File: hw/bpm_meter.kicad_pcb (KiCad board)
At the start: 2 copper layers, 55 x 73.5 mm, 92 parts, among them J1 weidmueller_SL5.08HC-06-90, J2 weidmueller_SL5.08HC-10-90, J901 USB_C_Receptacle_USB2.0, Q1 AO3400A, SW1 dip_switch_SPST16, SW901 SW_MEC_5E, U1 SP3485EN-L/TR, U2 AOZ1282CI, U901 RP2040, U902 AMS1117-3.3, U903 W25Q128JVS, Y901 Crystal_GND24_Small

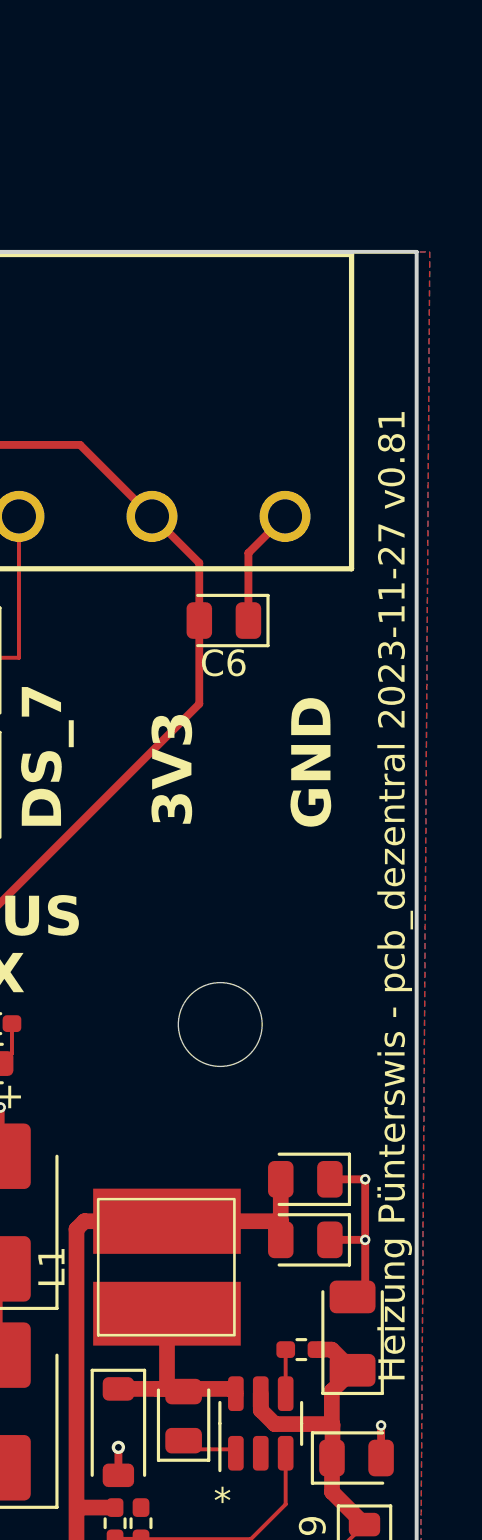
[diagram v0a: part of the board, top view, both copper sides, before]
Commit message: Renamed the KiCad project
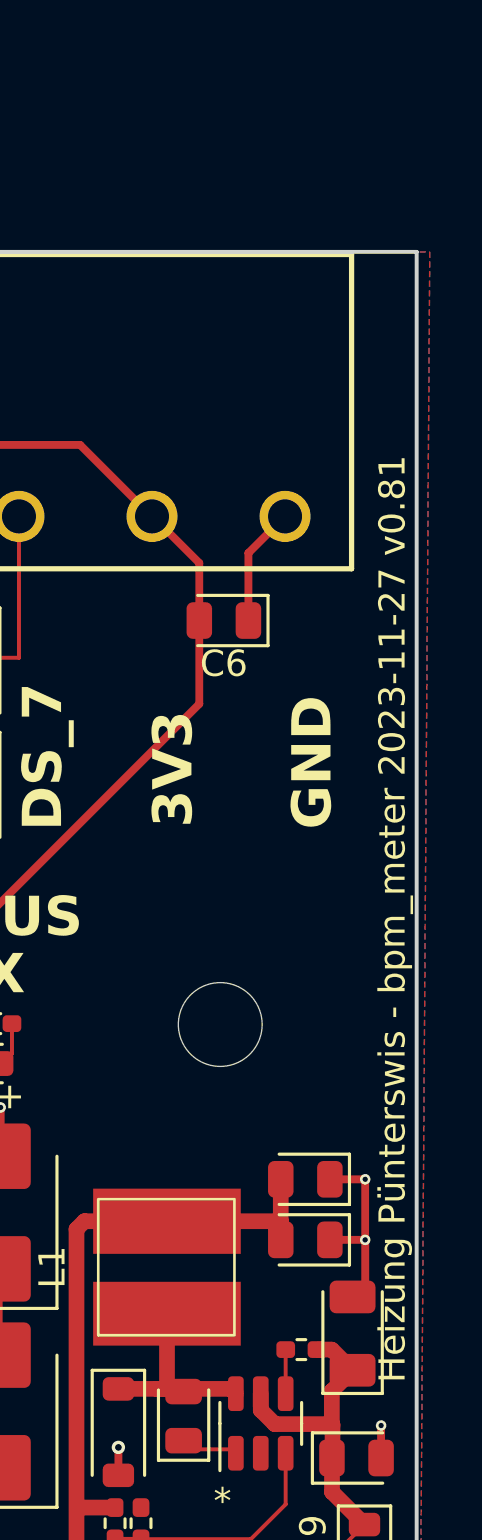
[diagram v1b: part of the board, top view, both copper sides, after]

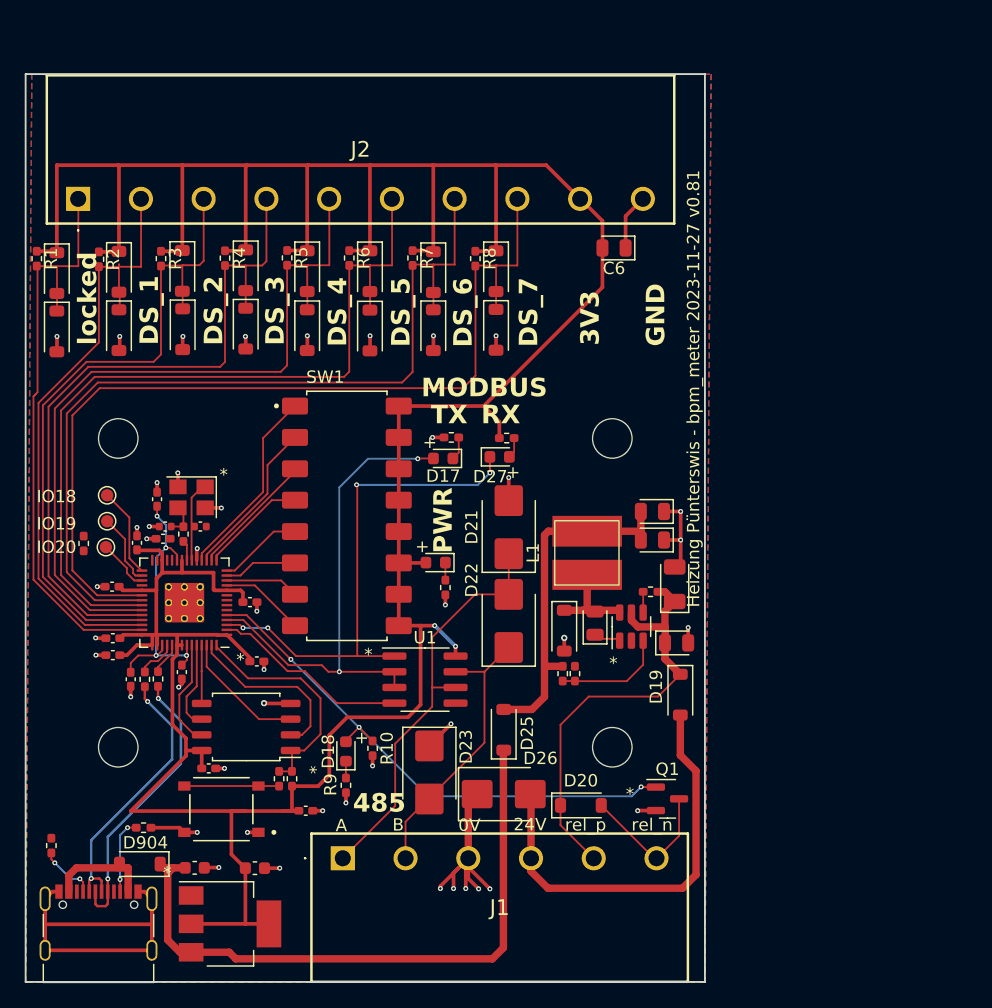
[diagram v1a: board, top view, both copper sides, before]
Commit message: Removed unused stuff and added beat input
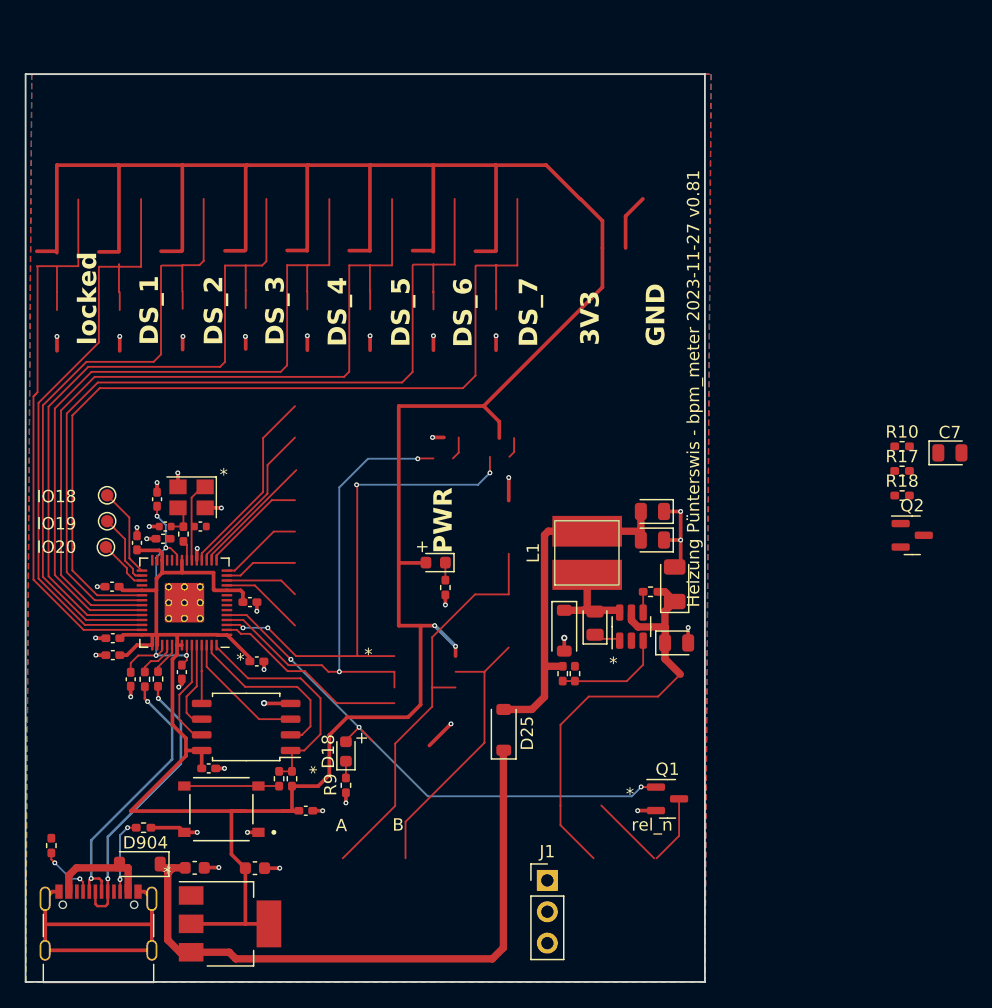
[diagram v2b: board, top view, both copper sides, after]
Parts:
- removed C6: 100n 50V, Diode_SMD:D_0805_2012Metric
- removed D1, D10, D11, D12, D13, D14, D15, D16, D19, D2, D20, D3, D4, D5, D6, D7, D8, D9: B5819W SL, Diode_SMD:D_SOD-123
- removed D17: LED RED, 00_project_library:LED_0603_1608Metric
- removed D21, D22, D23: SMBJ6.5CA, Diode_SMD:D_SMB
- removed D26: SMBJ30CA, Diode_SMD:D_SMB
- removed D27: LED BLUE, 00_project_library:LED_0603_1608Metric
- removed HOLDER1: ~, 00_project_library:din_rail_pcb_holder
- removed J2: weidmueller_SL5.08HC-10-90, 00_project_library:weidmueller_SL5.08HC-10-90
- removed R1, R14, R2, R3, R4, R5, R6, R7, R8: 4k7, Resistor_SMD:R_0402_1005Metric_Pad0.72x0.64mm_HandSolder
- removed R15, R16: 470R, Resistor_SMD:R_0402_1005Metric_Pad0.72x0.64mm_HandSolder
- removed SW1: dip_switch_SPST16, 00_project_library:dip_switch_SPST16
- removed U1: SP3485EN-L/TR, Package_SO:SOIC-8_3.9x4.9mm_P1.27mm
- added C7: 100n 50V, Diode_SMD:D_0805_2012Metric, F.Cu at (148.8, 89.7)
- added Q2: AO3400A, Package_TO_SOT_SMD:SOT-23, F.Cu at (145.8, 96.3)
- added R17: 10k, Resistor_SMD:R_0402_1005Metric_Pad0.72x0.64mm_HandSolder, F.Cu at (145.0, 91.1)
- added R18: 10k, Resistor_SMD:R_0402_1005Metric_Pad0.72x0.64mm_HandSolder, F.Cu at (145.0, 93.1)
- J1: value weidmueller_SL5.08HC-06-90 -> Conn_01x03_Pin; footprint 00_project_library:weidmueller_SL5.08HC-06-90 -> Connector_PinHeader_2.54mm:PinHeader_1x03_P2.54mm_Vertical
- R10: value 10k -> 4k7
- moved R10 49.4 mm to (145.0, 89.1), turned to 0 degrees
- moved J1 16.7 mm to (116.2, 124.3)
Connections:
- C1 pad 1: 24Vp -> +14V
- C2 pad 1: 24Vp -> +14V
- D18 pad 2: rel -> +5V
- J1 pad 1: 485_A -> +14V
- J1 pad 2: 485_B -> Net-(J1-Pin_2)
- Q1 pad 1: rel -> Net-(Q1-G)
- Q1 pad 3: rel_n -> beat_3V3
- R10 pad 1: rel -> Net-(Q1-G)
- R11 pad 1: 24Vp -> +14V
- R9 pad 2: GND -> Net-(Q2-D)
- U2 pad 5: 24Vp -> +14V
- U901 pad 11: modbus_addr_7 -> unconnected-(U901-GPIO8-Pad11)
- U901 pad 12: modbus_addr_6 -> unconnected-(U901-GPIO9-Pad12)
- U901 pad 13: modbus_addr_5 -> unconnected-(U901-GPIO10-Pad13)
- U901 pad 14: modbus_addr_4 -> unconnected-(U901-GPIO11-Pad14)
- U901 pad 15: modbus_addr_3 -> unconnected-(U901-GPIO12-Pad15)
- U901 pad 16: modbus_addr_2 -> unconnected-(U901-GPIO13-Pad16)
- U901 pad 17: modbus_addr_1 -> unconnected-(U901-GPIO14-Pad17)
- U901 pad 18: modbus_addr_0 -> unconnected-(U901-GPIO15-Pad18)
- U901 pad 2: MODBUS_DI -> beat_3V3
- U901 pad 3: MODBUS_RO -> unconnected-(U901-GPIO1-Pad3)
- U901 pad 34: ds_7 -> unconnected-(U901-GPIO22-Pad34)
- U901 pad 35: ds_6 -> unconnected-(U901-GPIO23-Pad35)
- U901 pad 36: ds_5 -> unconnected-(U901-GPIO24-Pad36)
- U901 pad 37: ds_4 -> unconnected-(U901-GPIO25-Pad37)
- U901 pad 38: ds_3 -> unconnected-(U901-GPIO26/ADC0-Pad38)
- U901 pad 39: ds_2 -> unconnected-(U901-GPIO27/ADC1-Pad39)
- U901 pad 4: MODBUS_DE -> unconnected-(U901-GPIO2-Pad4)
- U901 pad 40: ds_1 -> unconnected-(U901-GPIO28/ADC2-Pad40)
- U901 pad 41: ds_0 -> unconnected-(U901-GPIO29/ADC3-Pad41)
- U901 pad 5: rel -> unconnected-(U901-GPIO3-Pad5)
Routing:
- net (no net): track 0.00 -> 110.4 mm
- net unconnected-(U901-GPIO22-Pad34): track 0.00 -> 74.3 mm
- net ds_7: track 74.3 -> 0.00 mm
- net unconnected-(U901-GPIO23-Pad35): track 0.00 -> 70.3 mm
- net ds_6: track 70.3 -> 0.00 mm
- net unconnected-(U901-GPIO24-Pad36): track 0.00 -> 66.5 mm
- net ds_5: track 66.5 -> 0.00 mm
- net unconnected-(U901-GPIO25-Pad37): track 0.00 -> 62.5 mm
- net ds_4: track 62.5 -> 0.00 mm
- net unconnected-(U901-GPIO26/ADC0-Pad38): track 0.00 -> 58.2 mm
- net ds_3: track 58.2 -> 0.00 mm
- net unconnected-(U901-GPIO27/ADC1-Pad39): track 0.00 -> 53.8 mm
- net ds_2: track 53.8 -> 0.00 mm
- net unconnected-(U901-GPIO28/ADC2-Pad40): track 0.00 -> 50.1 mm
- net ds_1: track 50.1 -> 0.00 mm
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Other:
- board text removed: "0V"
- board text removed: "24V"
- board text removed: "485"
- board text removed: "MODBUS"
- board text removed: "RX"
- board text removed: "TX"
- board text removed: "rel_p"

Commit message: Export to PCB
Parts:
- removed D18: LED WHITE, 00_project_library:LED_0603_1608Metric
- removed IO18, IO19, IO20: TestPoint, TestPoint:TestPoint_Pad_D1.0mm
- added C10: 100n, Capacitor_SMD:C_0402_1005Metric, F.Cu at (215.6, 109.6)
- added C11: 1u, Capacitor_SMD:C_0402_1005Metric, F.Cu at (218.4, 101.7)
- added C12: 1u, Capacitor_SMD:C_0402_1005Metric, F.Cu at (218.4, 103.7)
- added C13: 100n, Capacitor_SMD:C_0402_1005Metric, F.Cu at (218.4, 105.7)
- added C14: 100n, Capacitor_SMD:C_0402_1005Metric, F.Cu at (218.4, 107.6)
- added C15: 1u, Capacitor_SMD:C_0402_1005Metric, F.Cu at (218.4, 109.6)
- added C16: 1u, Capacitor_SMD:C_0402_1005Metric, F.Cu at (221.3, 101.7)
- added C17: 100n, Capacitor_SMD:C_0402_1005Metric, F.Cu at (221.3, 103.7)
- added C18: 100n, Capacitor_SMD:C_0402_1005Metric, F.Cu at (221.3, 105.7)
- added C6: 1u, Capacitor_SMD:C_0402_1005Metric, F.Cu at (215.6, 101.7)
- added C8: 1u, Capacitor_SMD:C_0402_1005Metric, F.Cu at (215.6, 105.7)
- added C9: 100n, Capacitor_SMD:C_0402_1005Metric, F.Cu at (215.6, 107.6)
- added Q10: DMN2004VK, Package_TO_SOT_SMD:SOT-563, F.Cu at (223.5, 118.7)
- added Q11: DMN2004VK, Package_TO_SOT_SMD:SOT-563, F.Cu at (227.2, 112.2)
- added Q12: DMN2004VK, Package_TO_SOT_SMD:SOT-563, F.Cu at (227.2, 115.5)
- added Q13: DMN2004VK, Package_TO_SOT_SMD:SOT-563, F.Cu at (227.2, 118.7)
- added Q3: DMN2004VK, Package_TO_SOT_SMD:SOT-563, F.Cu at (216.0, 115.5)
- added Q4: DMN2004VK, Package_TO_SOT_SMD:SOT-563, F.Cu at (216.0, 118.7)
- added Q5: DMN2004VK, Package_TO_SOT_SMD:SOT-563, F.Cu at (219.8, 112.2)
- added Q6: DMN2004VK, Package_TO_SOT_SMD:SOT-563, F.Cu at (219.8, 115.5)
- added Q7: DMN2004VK, Package_TO_SOT_SMD:SOT-563, F.Cu at (219.8, 118.7)
- added Q8: DMN2004VK, Package_TO_SOT_SMD:SOT-563, F.Cu at (223.5, 112.2)
- added Q9: DMN2004VK, Package_TO_SOT_SMD:SOT-563, F.Cu at (223.5, 115.5)
- added R1: 4k7, Resistor_SMD:R_0402_1005Metric_Pad0.72x0.64mm_HandSolder, F.Cu at (215.8, 87.8)
- added R14: 220, Resistor_SMD:R_0402_1005Metric_Pad0.72x0.64mm_HandSolder, F.Cu at (219.0, 91.8)
- added R15: 220, Resistor_SMD:R_0402_1005Metric_Pad0.72x0.64mm_HandSolder, F.Cu at (219.0, 93.8)
- added R16: 220, Resistor_SMD:R_0402_1005Metric_Pad0.72x0.64mm_HandSolder, F.Cu at (219.0, 95.8)
- added R19: 220, Resistor_SMD:R_0402_1005Metric_Pad0.72x0.64mm_HandSolder, F.Cu at (219.0, 97.7)
- added R2: 220, Resistor_SMD:R_0402_1005Metric_Pad0.72x0.64mm_HandSolder, F.Cu at (215.8, 89.8)
- added R20: 220, Resistor_SMD:R_0402_1005Metric_Pad0.72x0.64mm_HandSolder, F.Cu at (219.0, 99.7)
- added R21: 220, Resistor_SMD:R_0402_1005Metric_Pad0.72x0.64mm_HandSolder, F.Cu at (222.2, 87.8)
- added R22: 220, Resistor_SMD:R_0402_1005Metric_Pad0.72x0.64mm_HandSolder, F.Cu at (222.2, 89.8)
- added R23: 220, Resistor_SMD:R_0402_1005Metric_Pad0.72x0.64mm_HandSolder, F.Cu at (222.2, 91.8)
- added R24: 220, Resistor_SMD:R_0402_1005Metric_Pad0.72x0.64mm_HandSolder, F.Cu at (222.2, 93.8)
- added R25: 220, Resistor_SMD:R_0402_1005Metric_Pad0.72x0.64mm_HandSolder, F.Cu at (222.2, 95.8)
- added R26: 220, Resistor_SMD:R_0402_1005Metric_Pad0.72x0.64mm_HandSolder, F.Cu at (222.2, 97.7)
- added R27: 220, Resistor_SMD:R_0402_1005Metric_Pad0.72x0.64mm_HandSolder, F.Cu at (222.2, 99.7)
- added R28: 220, Resistor_SMD:R_0402_1005Metric_Pad0.72x0.64mm_HandSolder, F.Cu at (225.5, 87.8)
- added R29: 220, Resistor_SMD:R_0402_1005Metric_Pad0.72x0.64mm_HandSolder, F.Cu at (225.5, 89.8)
- added R3: 220, Resistor_SMD:R_0402_1005Metric_Pad0.72x0.64mm_HandSolder, F.Cu at (215.8, 91.8)
- added R30: 220, Resistor_SMD:R_0402_1005Metric_Pad0.72x0.64mm_HandSolder, F.Cu at (225.5, 91.8)
- added R31: 220, Resistor_SMD:R_0402_1005Metric_Pad0.72x0.64mm_HandSolder, F.Cu at (225.5, 93.8)
- added R4: 220, Resistor_SMD:R_0402_1005Metric_Pad0.72x0.64mm_HandSolder, F.Cu at (215.8, 93.8)
- added R5: 220, Resistor_SMD:R_0402_1005Metric_Pad0.72x0.64mm_HandSolder, F.Cu at (215.8, 95.8)
- added R6: 220, Resistor_SMD:R_0402_1005Metric_Pad0.72x0.64mm_HandSolder, F.Cu at (215.8, 97.7)
- added R7: 220, Resistor_SMD:R_0402_1005Metric_Pad0.72x0.64mm_HandSolder, F.Cu at (215.8, 99.7)
- added R8: 220, Resistor_SMD:R_0402_1005Metric_Pad0.72x0.64mm_HandSolder, F.Cu at (219.0, 87.8)
- added U1: SLS0391FR1A1GD, 00_project_library:SLS0391, F.Cu at (223.2, 59.2)
- added U3: H11L1, 00_project_library:SOP-6-2.54mm, F.Cu at (164.2, 120.7)
- added U4: SLS0391FR1A1GD, 00_project_library:SLS0391, F.Cu at (223.2, 70.2)
- added U5: SLS0391FR1A1GD, 00_project_library:SLS0391, F.Cu at (223.2, 81.3)
- C7: value 100n 50V -> 100n; footprint Diode_SMD:D_0805_2012Metric -> Capacitor_SMD:C_0402_1005Metric
- J1: footprint Connector_PinHeader_2.54mm:PinHeader_1x03_P2.54mm_Vertical -> Connector_PinHeader_2.54mm:PinHeader_1x05_P2.54mm_Vertical
- Q2: value AO3400A -> DMN2004VK; footprint Package_TO_SOT_SMD:SOT-23 -> Package_TO_SOT_SMD:SOT-563
- R9: value 470 -> 220
- moved R9 122.0 mm to (219.0, 89.8), turned to 0 degrees
- moved Q2 72.0 mm to (216.0, 112.2)
- moved C7 68.2 mm to (215.6, 103.7)
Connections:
- C7 pad 1: Net-(Q1-G) -> +5V
- J1 pad 3: GND -> Net-(J1-Pin_3)
- Q1 pad 3: beat_3V3 -> beat_od
- Q2 pad 1: beat_3V3 -> GND
- Q2 pad 2: GND -> led_1A
- Q2 pad 3: Net-(Q2-D) -> Net-(Q2-D2)
- R17 pad 1: Net-(J1-Pin_2) -> Net-(Q1-G)
- R17 pad 2: Net-(Q1-G) -> Net-(J1-Pin_2)
- R18 pad 2: beat_3V3 -> beat_od
- R9 pad 2: Net-(Q2-D) -> Net-(Q5-D2)
- U901 pad 11: unconnected-(U901-GPIO8-Pad11) -> led_2A
- U901 pad 12: unconnected-(U901-GPIO9-Pad12) -> led_2B
- U901 pad 13: unconnected-(U901-GPIO10-Pad13) -> led_2C
- U901 pad 14: unconnected-(U901-GPIO11-Pad14) -> led_2D
- U901 pad 15: unconnected-(U901-GPIO12-Pad15) -> led_2E
- U901 pad 16: unconnected-(U901-GPIO13-Pad16) -> led_2F
- U901 pad 17: unconnected-(U901-GPIO14-Pad17) -> led_2G
- U901 pad 18: unconnected-(U901-GPIO15-Pad18) -> led_2P
- U901 pad 2: beat_3V3 -> led_1A
- U901 pad 27: unconnected-(U901-GPIO16-Pad27) -> led_3A
- U901 pad 28: unconnected-(U901-GPIO17-Pad28) -> led_3B
- U901 pad 29: Net-(U901-GPIO18) -> led_3C
- U901 pad 3: unconnected-(U901-GPIO1-Pad3) -> led_1B
- U901 pad 30: Net-(U901-GPIO19) -> led_3D
- U901 pad 31: Net-(U901-GPIO20) -> led_3E
- U901 pad 32: unconnected-(U901-GPIO21-Pad32) -> led_3F
- U901 pad 34: unconnected-(U901-GPIO22-Pad34) -> led_3G
- U901 pad 35: unconnected-(U901-GPIO23-Pad35) -> led_3P
- U901 pad 36: unconnected-(U901-GPIO24-Pad36) -> beat_od
- U901 pad 37: unconnected-(U901-GPIO25-Pad37) -> beat_opto
- U901 pad 4: unconnected-(U901-GPIO2-Pad4) -> led_1C
- U901 pad 5: unconnected-(U901-GPIO3-Pad5) -> led_1D
- U901 pad 6: unconnected-(U901-GPIO4-Pad6) -> led_1E
- U901 pad 7: unconnected-(U901-GPIO5-Pad7) -> led_1F
- U901 pad 8: unconnected-(U901-GPIO6-Pad8) -> led_1G
- U901 pad 9: unconnected-(U901-GPIO7-Pad9) -> led_1P
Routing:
- net +3V3: track 282.5 -> 138.8 mm
- net unconnected-(U901-GPIO22-Pad34): track 74.3 -> 0.00 mm
- net unconnected-(U901-GPIO23-Pad35): track 70.3 -> 0.00 mm
- net unconnected-(U901-GPIO24-Pad36): track 66.5 -> 0.00 mm
- net unconnected-(U901-GPIO25-Pad37): track 62.5 -> 0.00 mm
- net unconnected-(U901-GPIO1-Pad3): track 41.0 -> 0.00 mm, vias 4 -> 0
- net unconnected-(U901-GPIO2-Pad4): track 40.1 -> 0.00 mm, vias 2 -> 0
- net unconnected-(U901-GPIO26/ADC0-Pad38): track 58.2 -> 22.6 mm
- net unconnected-(U901-GPIO27/ADC1-Pad39): track 53.8 -> 23.3 mm
- net beat_od: track 0.00 -> 26.5 mm
- net unconnected-(U901-GPIO28/ADC2-Pad40): track 50.1 -> 24.2 mm
- net unconnected-(U901-GPIO29/ADC3-Pad41): track 48.2 -> 25.3 mm
- net beat_opto: track 0.00 -> 21.7 mm
- net beat_3V3: track 21.6 -> 0.00 mm
- net led_3P: track 0.00 -> 19.9 mm
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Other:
- board text removed: "3V3"
- board text removed: "DS_1"
- board text removed: "DS_2"
- board text removed: "DS_3"
- board text removed: "DS_4"
- board text removed: "DS_5"
- board text removed: "DS_6"
- board text removed: "DS_7"
- board text removed: "GND"
- board text removed: "locked"
- board text removed: "rel_n"
